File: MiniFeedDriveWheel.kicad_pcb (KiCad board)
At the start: 2 copper layers, 32 x 32 mm, 0 parts

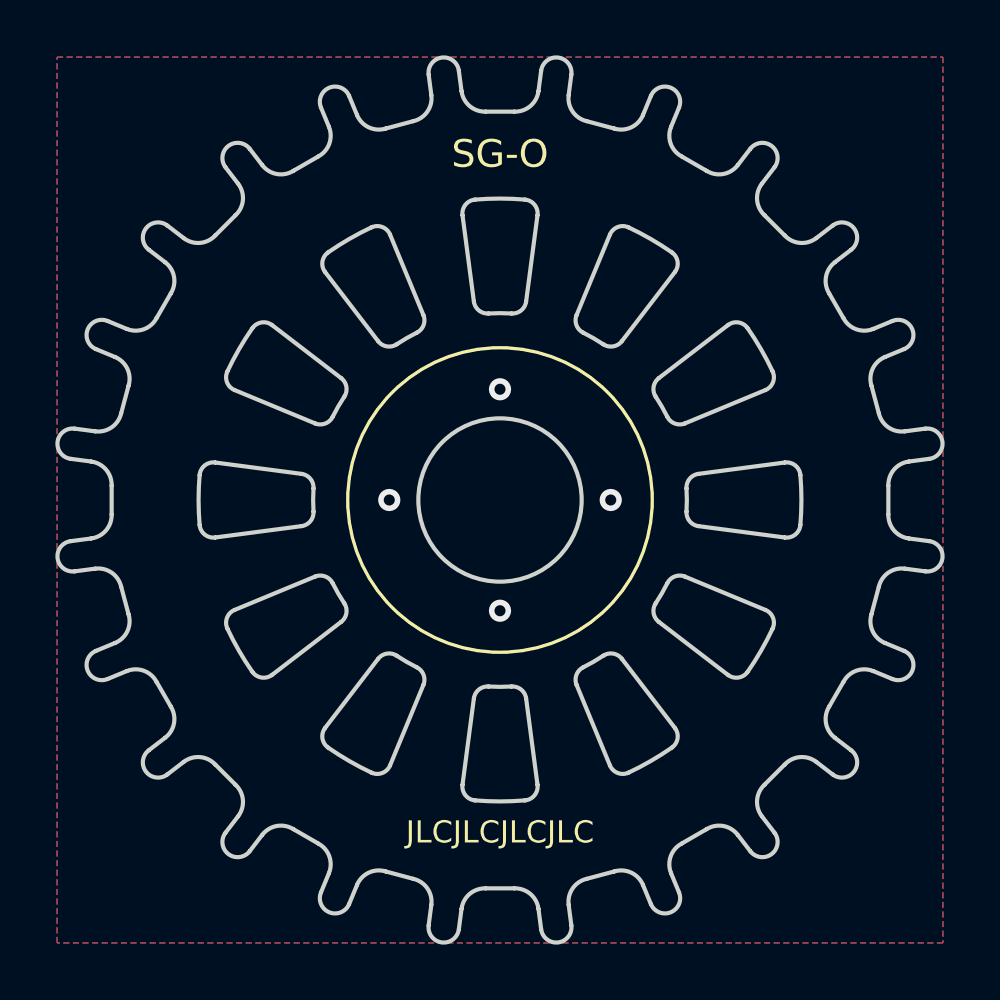
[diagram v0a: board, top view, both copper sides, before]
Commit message: Added to high resolution drive wheel Bump to v0.3
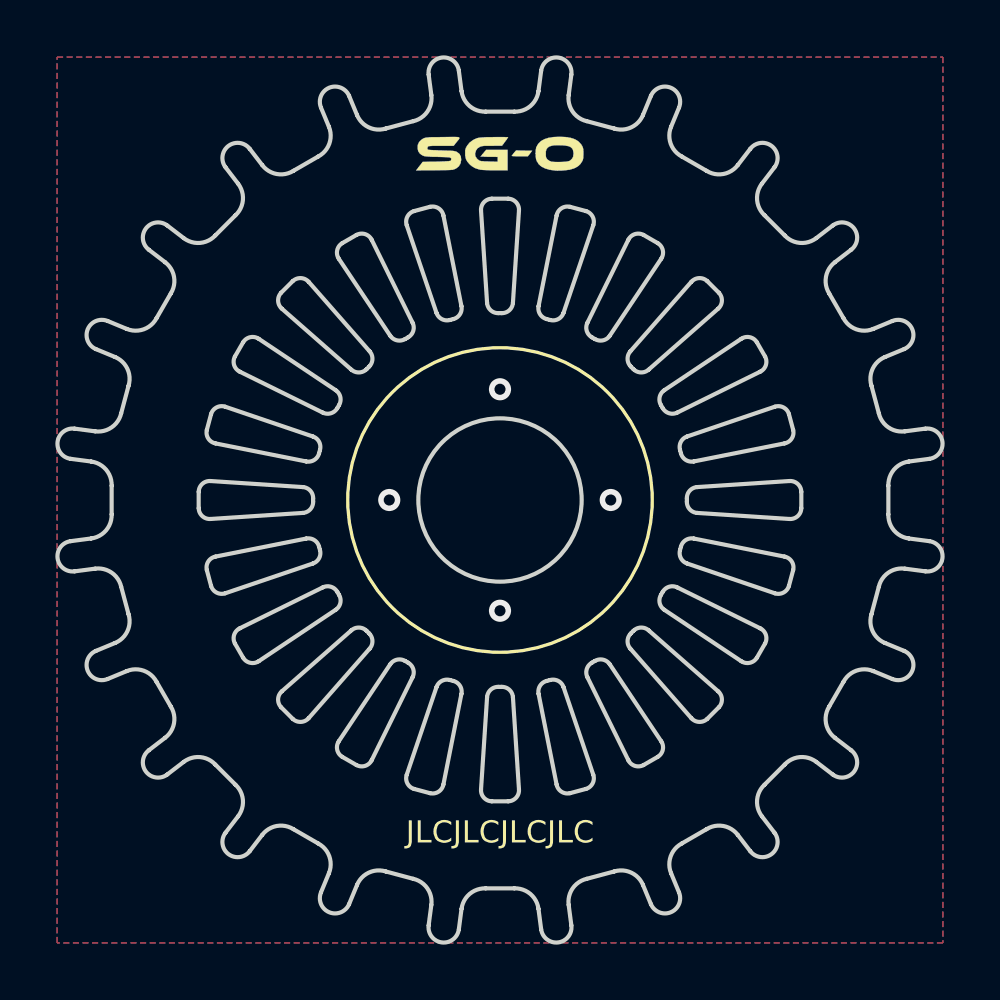
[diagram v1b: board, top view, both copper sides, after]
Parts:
- added G***: LOGO, global:Logo_SG-O_mini, F.Cu at (100.0, 87.5)
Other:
- outline, holes or cut-outs redrawn
- board text added: "High Resolution"
- board text added: "v0.3"
- board text removed: "SG-O"
- board text removed: "v0.2"
